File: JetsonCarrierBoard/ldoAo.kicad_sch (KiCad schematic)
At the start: 1 part

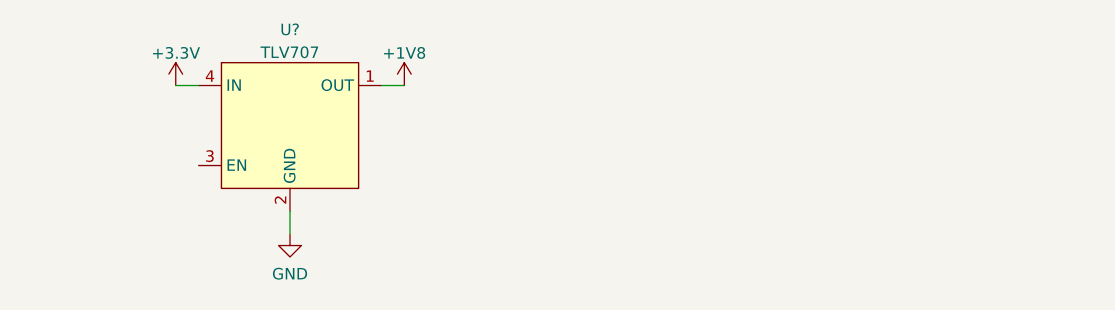
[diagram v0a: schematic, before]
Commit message: Power Sequencing Wiring Part 1
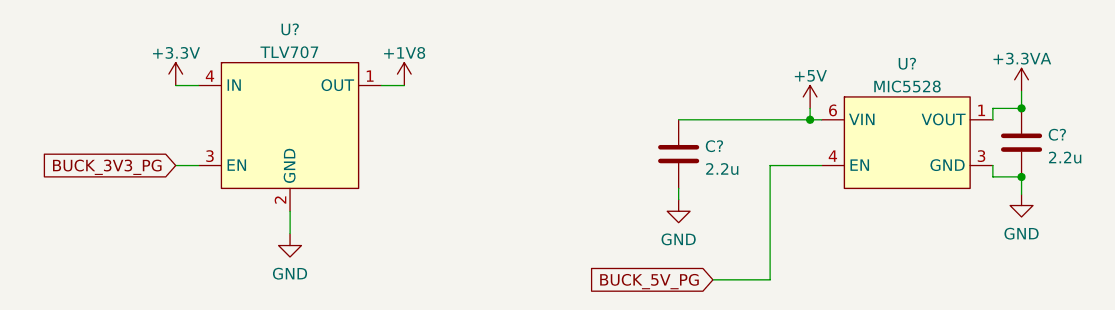
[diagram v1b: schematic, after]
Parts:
- added C? (x2): 2.2u, symbol Device:C
- added U?: MIC5528, symbol Voltage_Regulators_Linear:MIC5528
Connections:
- net GND: now also C?.2, C?.2, U?.3 (GND)
- net BUCK_3V3_PG: now reaches U?.3 (EN)
- new net +3.3VA: C?.1, U?.1 (VOUT)
- new net +5V: C?.1, U?.6 (VIN)
- new net BUCK_5V_PG: U?.4 (EN)
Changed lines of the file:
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@@
 (kicad_sch (version 20211123) (generator eeschema)
   (paper "A4")
+  (junction (at 151.13 63.5) (diameter 0) (color 0 0 0 0)
+  )
+  (junction (at 127.635 57.15) (diameter 0) (color 0 0 0 0)
+  )
+  (junction (at 151.13 55.88) (diameter 0) (color 0 0 0 0)
+  )
+  (wire (pts (xy 57.15 62.23) (xy 59.69 62.23))
+    (stroke (width 0) (type default) (color 0 0 0 0))
+  )
   (wire (pts (xy 80.01 53.34) (xy 82.55 53.34))
     (stroke (width 0) (type default) (color 0 0 0 0))
   )
+  (wire (pts (xy 147.955 55.88) (xy 151.13 55.88))
+    (stroke (width 0) (type default) (color 0 0 0 0))
+  )
+  (wire (pts (xy 147.955 62.23) (xy 147.955 63.5))
+    (stroke (width 0) (type default) (color 0 0 0 0))
+  )
+  (wire (pts (xy 123.19 74.93) (xy 123.19 62.23))
+    (stroke (width 0) (type default) (color 0 0 0 0))
+  )
+  (wire (pts (xy 113.03 57.15) (xy 127.635 57.15))
+    (stroke (width 0) (type default) (color 0 0 0 0))
+  )
+  (wire (pts (xy 116.84 74.93) (xy 123.19 74.93))
+    (stroke (width 0) (type default) (color 0 0 0 0))
+  )
+  (wire (pts (xy 147.955 57.15) (xy 147.955 55.88))
+    (stroke (width 0) (type default) (color 0 0 0 0))
+  )
   (wire (pts (xy 57.15 53.34) (xy 59.69 53.34))
     (stroke (width 0) (type default) (color 0 0 0 0))
   )
+  (wire (pts (xy 127.635 55.88) (xy 127.635 57.15))
+    (stroke (width 0) (type default) (color 0 0 0 0))
+  )
+  (wire (pts (xy 151.13 53.975) (xy 151.13 55.88))
+    (stroke (width 0) (type default) (color 0 0 0 0))
+  )
   (wire (pts (xy 69.85 67.31) (xy 69.85 69.85))
     (stroke (width 0) (type default) (color 0 0 0 0))
+  )
+  (wire (pts (xy 127.635 57.15) (xy 128.905 57.15))
+    (stroke (width 0) (type default) (color 0 0 0 0))
+  )
+  (wire (pts (xy 147.955 63.5) (xy 151.13 63.5))
+    (stroke (width 0) (type default) (color 0 0 0 0))
+  )
+  (wire (pts (xy 123.19 62.23) (xy 128.905 62.23))
+    (stroke (width 0) (type default) (color 0 0 0 0))
+  )
+  (wire (pts (xy 151.13 63.5) (xy 151.13 65.405))
+    (stroke (width 0) (type default) (color 0 0 0 0))
+  )
+  (wire (pts (xy 113.03 64.77) (xy 113.03 66.04))
+    (stroke (width 0) (type default) (color 0 0 0 0))
+  )
+  (global_label "BUCK_5V_PG" (shape input) (at 116.84 74.93 180) (fields_autoplaced)
+    (effects (font (size 1.27 1.27)) (justify right))
+    (property "Intersheet References" "${INTERSHEET_REFS}" (id 0) (at 102.5131 74.8506 0)
+      (effects (font (size 1.27 1.27)) (justify right) hide)
+    )
+  )
+  (global_label "BUCK_3V3_PG" (shape input) (at 57.15 62.23 180) (fields_autoplaced)
+    (effects (font (size 1.27 1.27)) (justify right))
+    (property "Intersheet References" "${INTERSHEET_REFS}" (id 0) (at 41.6136 62.1506 0)
+      (effects (font (size 1.27 1.27)) (justify right) hide)
+    )
+  )
+  (symbol (lib_id "Device:C") (at 113.03 60.96 0) (unit 1)
+    (in_bom yes) (on_board yes) (fields_autoplaced)
+    (property "Reference" "C?" (id 0) (at 115.951 60.1253 0)
+      (effects (font (size 1.27 1.27)) (justify left))
+    )
+    (property "Value" "2.2u" (id 1) (at 115.951 62.6622 0)
+      (effects (font (size 1.27 1.27)) (justify left))
+    )
+    (property "Footprint" "" (id 2) (at 113.9952 64.77 0)
+      (effects (font (size 1.27 1.27)) hide)
+    )
+    (property "Datasheet" "~" (id 3) (at 113.03 60.96 0)
+      (effects (font (size 1.27 1.27)) hide)
+    )
+    (pin "1")
+    (pin "2")
+  )
+  (symbol (lib_id "power:+5V") (at 127.635 55.88 0) (unit 1)
+    (in_bom yes) (on_board yes) (fields_autoplaced)
+    (property "Reference" "#PWR?" (id 0) (at 127.635 59.69 0)
+      (effects (font (size 1.27 1.27)) hide)
+    )
+    (property "Value" "+5V" (id 1) (at 127.635 52.3042 0))
+    (property "Footprint" "" (id 2) (at 127.635 55.88 0)
+      (effects (font (size 1.27 1.27)) hide)
+    )
+    (property "Datasheet" "" (id 3) (at 127.635 55.88 0)
+      (effects (font (size 1.27 1.27)) hide)
+    )
+    (pin "1")
+  )
+  (symbol (lib_id "Voltage_Regulators_Linear:MIC5528") (at 137.795 54.61 0) (unit 1)
+    (in_bom yes) (on_board yes) (fields_autoplaced)
+    (property "Reference" "U?" (id 0) (at 138.43 50.961 0))
+    (property "Value" "MIC5528" (id 1) (at 138.43 53.4979 0))
+    (property "Footprint" "" (id 2) (at 137.795 54.61 0)
+      (effects (font (size 1.27 1.27)) hide)
+    )
+    (property "Datasheet" "" (id 3) (at 137.795 54.61 0)
+      (effects (font (size 1.27 1.27)) hide)
+    )
+    (pin "1")
+    (pin "2")
+    (pin "3")
+    (pin "4")
+    (pin "5")
+    (pin "6")
   )
   (symbol (lib_id "power:+1V8") (at 82.55 53.34 0) (unit 1)
@@
     )
     (property "Datasheet" "" (id 3) (at 82.55 53.34 0)
+      (effects (font (size 1.27 1.27)) hide)
+    )
+    (pin "1")
+  )
+  (symbol (lib_id "power:GND") (at 151.13 65.405 0) (unit 1)
+    (in_bom yes) (on_board yes) (fields_autoplaced)
+    (property "Reference" "#PWR?" (id 0) (at 151.13 71.755 0)
+      (effects (font (size 1.27 1.27)) hide)
+    )
+    (property "Value" "GND" (id 1) (at 151.13 69.8484 0))
+    (property "Footprint" "" (id 2) (at 151.13 65.405 0)
+      (effects (font (size 1.27 1.27)) hide)
+    )
+    (property "Datasheet" "" (id 3) (at 151.13 65.405 0)
       (effects (font (size 1.27 1.27)) hide)
     )
@@
     (pin "4")
   )
+  (symbol (lib_id "Device:C") (at 151.13 59.69 0) (unit 1)
+    (in_bom yes) (on_board yes) (fields_autoplaced)
+    (property "Reference" "C?" (id 0) (at 154.051 58.8553 0)
+      (effects (font (size 1.27 1.27)) (justify left))
+    )
+    (property "Value" "2.2u" (id 1) (at 154.051 61.3922 0)
+      (effects (font (size 1.27 1.27)) (justify left))
+    )
+    (property "Footprint" "" (id 2) (at 152.0952 63.5 0)
+      (effects (font (size 1.27 1.27)) hide)
+    )
+    (property "Datasheet" "~" (id 3) (at 151.13 59.69 0)
+      (effects (font (size 1.27 1.27)) hide)
+    )
+    (pin "1")
+    (pin "2")
+  )
+  (symbol (lib_id "power:+3.3VA") (at 151.13 53.975 0) (unit 1)
+    (in_bom yes) (on_board yes) (fields_autoplaced)
+    (property "Reference" "#PWR?" (id 0) (at 151.13 57.785 0)
+      (effects (font (size 1.27 1.27)) hide)
+    )
+    (property "Value" "+3.3VA" (id 1) (at 151.13 50.3992 0))
+    (property "Footprint" "" (id 2) (at 151.13 53.975 0)
+      (effects (font (size 1.27 1.27)) hide)
+    )
+    (property "Datasheet" "" (id 3) (at 151.13 53.975 0)
+      (effects (font (size 1.27 1.27)) hide)
+    )
+    (pin "1")
+  )
   (symbol (lib_id "power:+3.3V") (at 57.15 53.34 0) (unit 1)
     (in_bom yes) (on_board yes) (fields_autoplaced)
@@
       (effects (font (size 1.27 1.27)) hide)
     )
+    (pin "1")
+  )
+  (symbol (lib_id "power:GND") (at 113.03 66.04 0) (unit 1)
+    (in_bom yes) (on_board yes) (fields_autoplaced)
+    (property "Reference" "#PWR?" (id 0) (at 113.03 72.39 0)
+      (effects (font (size 1.27 1.27)) hide)
+    )
+    (property "Value" "GND" (id 1) (at 113.03 70.4834 0))
+    (property "Footprint" "" (id 2) (at 113.03 66.04 0)
+      (effects (font (size 1.27 1.27)) hide)
+    )
+    (property "Datasheet" "" (id 3) (at 113.03 66.04 0)
+      (effects (font (size 1.27 1.27)) hide)
+    )

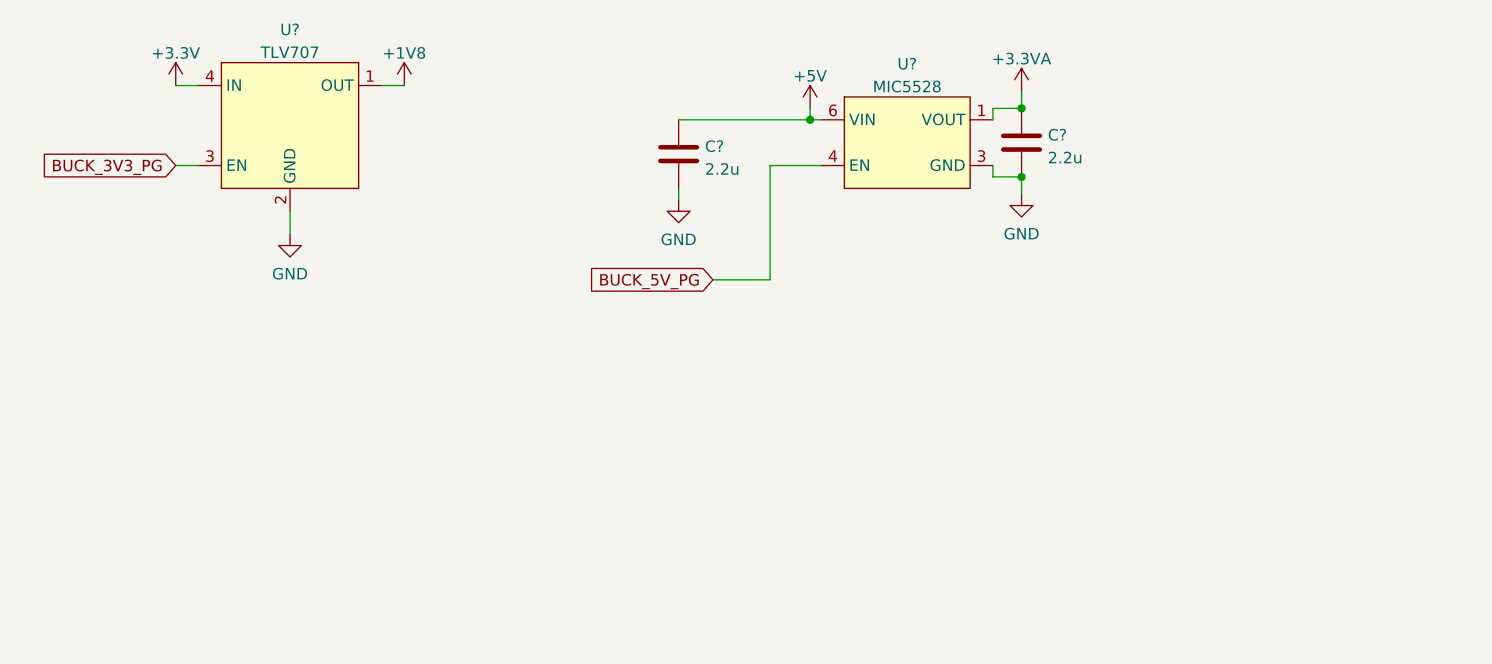
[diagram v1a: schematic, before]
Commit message: Adding more Title block info and changing main hierarchical page layout
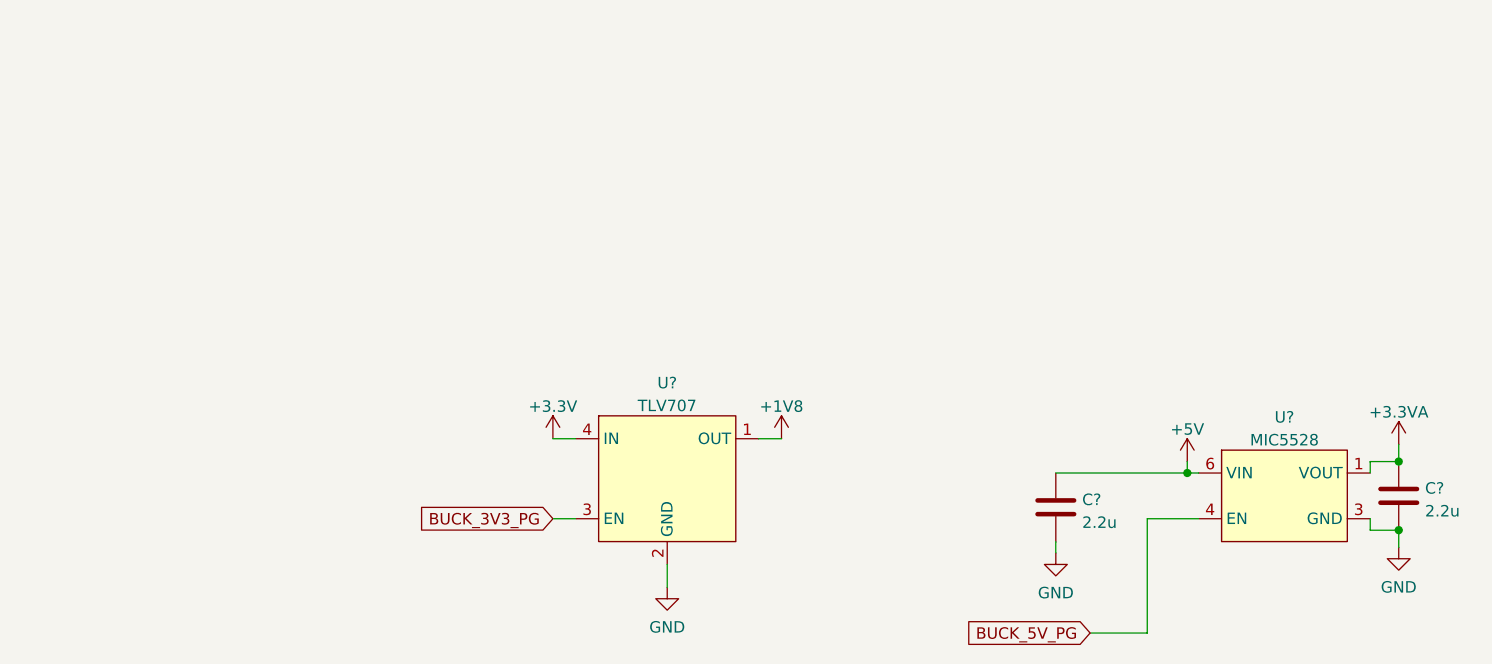
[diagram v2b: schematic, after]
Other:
- title: (none) -> 1V8 LDO & 3V3 AO Rails
- moved on the sheet: C?, U?
